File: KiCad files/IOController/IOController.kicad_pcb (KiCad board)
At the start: 2 copper layers, 30 x 74.3 mm, 48 parts, among them IC1 TPS922054DMTR, J1 AVR-ISP-6, J2 XT60 Horizontal Socket, J3 edge connector, Q1 BSS138, SW1 RotaryEncoder_Switch, SW2 TL3342, U1 LP2985-1.8, U3 LP2985-5.0, U4 ATtiny45V-10X

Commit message: updated small changes
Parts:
- added NT1: NetTie, NetTie:NetTie-2_SMD_Pad2.0mm, F.Cu at (37.0, 32.4)
- added R12: 0Ω 0402, Resistor_SMD:R_0402_1005Metric, F.Cu at (20.9, 39.2)
- added R13: 0Ω 0402, Resistor_SMD:R_0402_1005Metric, F.Cu at (21.9, 39.2)
- C14: value 25V 100nF 0402 -> 50V 0.1uF 0805; footprint Capacitor_SMD:C_0402_1005Metric -> Capacitor_SMD:C_0805_2012Metric
- C17: value 16V 2.2uF 0402 -> Csense 50V 2.2uF 0805; footprint Capacitor_SMD:C_0402_1005Metric -> Capacitor_SMD:C_0805_2012Metric
- IC1: value TPS922054DMTR -> TPS923654DMTR
- J1: footprint Connector_PinHeader_1.00mm:PinHeader_2x03_P1.00mm_Vertical -> Connector_PinHeader_2.54mm:PinHeader_2x03_P2.54mm_Vertical
- L1: value VLS6045AF-100M -> SRP1770TA-220M; footprint Inductor_SMD:L_TDK_VLS6045EX_VLS6045AF -> Inductor_SMD:L_Bourns_SRP1770TA_16.9x16.9mm
- R10: value 309K 0402 -> Rovp1 232K 0402
- R11: value 102K 0402 -> Rovp2 10K 0402
- R6: value 52K3 0402 -> Rfset 52K3 0402
- R7: value 61K9 0402 -> Rtemp 61K9 0402
- R8: value 825ohm 0402 -> Rcomp 825ohm 0402
- R9: value 33mΩ 2512 -> Rsense 65mΩ 2512
- SW2: value TL3342 -> B3U; footprint Button_Switch_SMD:SW_SPST_TL3342 -> Button_Switch_SMD:SW_SPST_B3U-1000P-B
- moved C14 22.7 mm to (19.4, 38.5), turned to 90 degrees
- moved C12 22.1 mm to (22.1, 48.6), turned to 180 degrees
- moved R10 21.1 mm to (22.1, 37.8)
- moved C13 20.9 mm to (23.5, 50.0)
- moved R5 20.9 mm to (24.5, 50.0)
- moved R11 20.5 mm to (24.0, 37.8), turned to 180 degrees
- moved IC1 20.3 mm to (23.2, 46.0)
- moved R8 18.3 mm to (23.5, 41.2)
- moved C17 18.3 mm to (17.4, 38.5), turned to 90 degrees
- moved C15 18.0 mm to (24.0, 38.8)
- moved C16 18.0 mm to (24.0, 39.7)
- moved R6 17.5 mm to (24.5, 41.2), turned to 90 degrees
- moved R7 16.5 mm to (25.5, 41.2), turned to 90 degrees
- moved R9 16.1 mm to (19.8, 34.8), turned to 180 degrees
- moved D1 13.7 mm to (17.4, 45.5), turned to 0 degrees
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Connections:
- C14 pad 1: Net-(IC1-CSN) -> Net-(D1-K)
- C14 pad 2: LED_V- -> LED V+
- C17 pad 1: Net-(IC1-CSN) -> Net-(D1-K)
- C17 pad 2: LED_V- -> LED V+
- C18 pad 1: VCC -> LED V+
- C19 pad 1: VCC -> LED V+
- C20 pad 1: VCC -> LED V+
- C21 pad 1: VCC -> LED V+
- C22 pad 1: VCC -> LED V+
- C23 pad 1: VCC -> LED V+
- D1 pad 3: VCC -> Net-(D1-K)
- IC1 pad 12: LED_V- -> Net-(IC1-CSP)
- J1 pad 3: ROT_A -> SW1
- J3 pad 1: VCC -> LED V+
- L1 pad 1: Net-(IC1-SW) -> VCC
- L1 pad 2: Net-(IC1-CSN) -> Net-(IC1-SW)
- R10 pad 2: LED_V- -> LED V+
- R9 pad 1: Net-(IC1-CSN) -> Net-(D1-K)
- R9 pad 2: LED_V- -> LED V+
- U4 pad 3: SW1 -> ROT_A
- U4 pad 7: ROT_A -> SW1
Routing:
- net LED V+: track 0.00 -> 41.0 mm, vias 0 -> 2
- net Net-(D1-K): track 0.00 -> 23.9 mm, vias 0 -> 3
- net Net-(IC1-CSN): track 27.4 -> 5.20 mm
- net SW1: track 20.0 -> 38.3 mm, vias 2 -> 4
- net ROT_SW1: track 29.4 -> 46.3 mm
- net +1V8: track 36.8 -> 53.6 mm
- net VCC: track 101.9 -> 85.8 mm, vias 341 -> 0
- net Net-(IC1-FSET): track 18.3 -> 2.85 mm
- net GND: track 9.53 -> 22.3 mm, vias 205 -> 22
- net Net-(IC1-TEMP): track 15.8 -> 2.98 mm
- net LED_V-: track 34.3 -> 23.7 mm
- net Net-(IC1-COMP): track 12.4 -> 2.98 mm
- net Net-(IC1-SW): track 14.9 -> 23.2 mm, vias 0 -> 2
- net Net-(J1-~{RST}): track 3.56 -> 11.1 mm, vias 0 -> 2
- net Net-(C15-Pad1): track 8.88 -> 1.94 mm
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- removed copper zone on F.Cu, net LED_V-
- removed copper zone on B.Cu, net VCC
- removed copper zone on F.Cu, net VCC

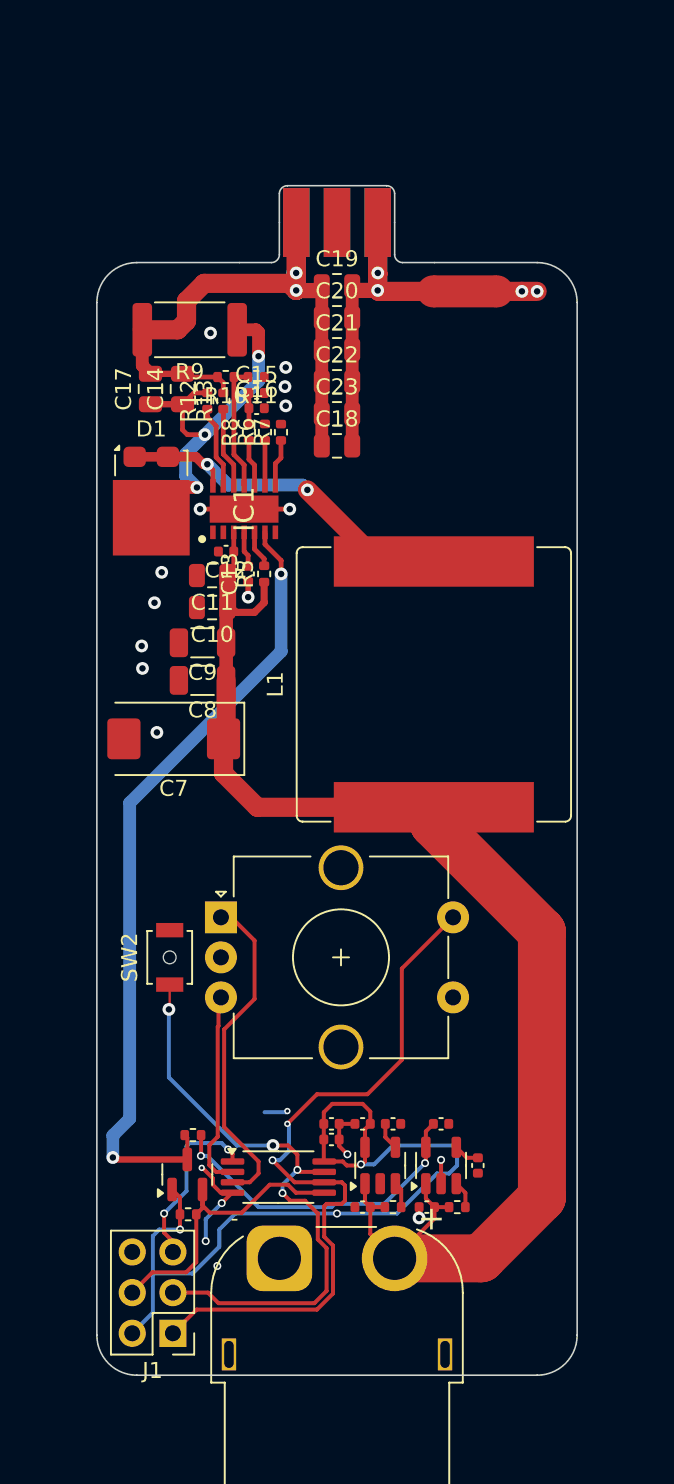
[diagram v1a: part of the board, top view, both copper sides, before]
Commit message: re-organised some files, started work on implementing 100W and 240W EPR versions of the charge board
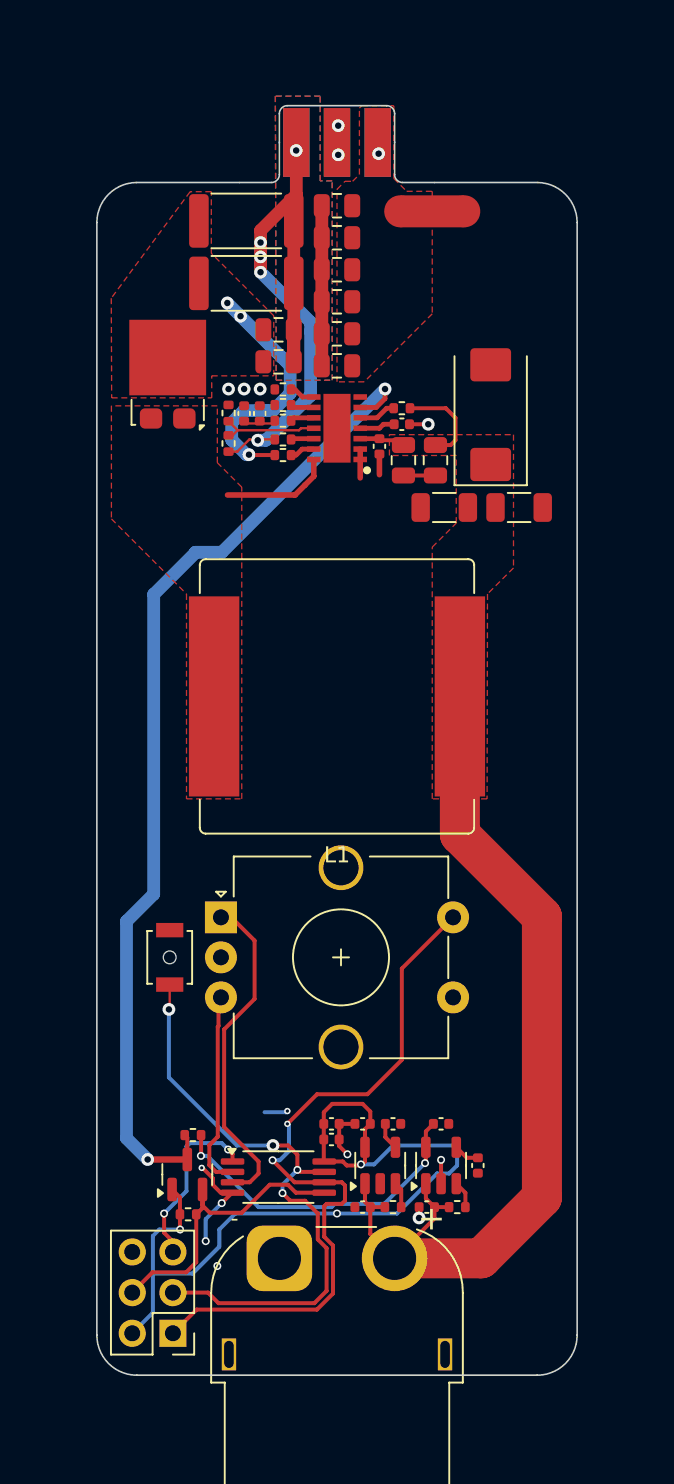
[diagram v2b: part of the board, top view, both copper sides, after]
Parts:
- added R14: 2512 120mR, Resistor_SMD:R_2512_6332Metric, F.Cu at (23.3, 31.9)
- C17: value Csense 50V 2.2uF 0805 -> Csense 50V 30uF 0805
- R10: value Rovp1 232K 0402 -> Rovp1 200K 0402
- R6: value Rfset 52K3 0402 -> Rfset 160K 0402
- R7: value Rtemp 61K9 0402 -> Rtemp 57K6 0402
- R9: value Rsense 65mΩ 2512 -> 2512 120mR
- moved C7 28.3 mm to (38.6, 40.1), turned to 90 degrees
- moved C9 21.5 mm to (40.4, 45.9), turned to 0 degrees
- moved C8 18.6 mm to (35.7, 45.9)
- moved C10 16.7 mm to (35.1, 43.0), turned to -90 degrees
- moved C11 14.0 mm to (33.1, 43.0), turned to -90 degrees
- moved R5 13.5 mm to (33.0, 39.7), turned to 180 degrees
- moved C13 13.4 mm to (33.0, 40.7), turned to 180 degrees
- moved C12 11.6 mm to (31.6, 42.1), turned to -90 degrees
- moved C17 8.81 mm to (25.4, 34.8), turned to 0 degrees
- moved D1 7.99 mm to (18.4, 37.6), turned to 180 degrees
- moved IC1 7.69 mm to (29.0, 41.0), turned to 180 degrees
- moved R9 7.67 mm to (23.3, 28.0), turned to 0 degrees
- moved C14 6.24 mm to (25.4, 36.8), turned to 0 degrees
- moved L1 6.10 mm to (29.0, 57.7), turned to 180 degrees
- moved R12 5.81 mm to (25.6, 42.6), turned to 180 degrees
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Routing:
- net LED_V-: track 23.7 -> 0.00 mm, vias 2 -> 1
- net VCC: track 85.8 -> 66.1 mm
- net Net-(IC1-SW): track 23.2 -> 6.92 mm, vias 2 -> 0
- net LED_PWM_5V: track 50.1 -> 62.8 mm
- net Net-(D1-K): track 23.9 -> 15.8 mm
- net LED V+: track 41.0 -> 48.8 mm, vias 2 -> 5
- net Net-(IC1-CSN): track 5.20 -> 1.57 mm
- net Net-(IC1-CSP): track 5.06 -> 1.44 mm
- net GND: track 22.3 -> 19.5 mm, vias 22 -> 12
- net Net-(IC1-UVP): track 7.95 -> 6.31 mm
- net Net-(IC1-COMP): track 2.98 -> 1.49 mm
- net Net-(IC1-TEMP): track 2.98 -> 1.61 mm
- net Net-(IC1-FSET): track 2.85 -> 1.48 mm
- net unconnected-(J3-Pin_2-Pad2): vias 0 -> 2
- added copper zone on B.Cu, net LED V+
- added copper zone on F.Cu, net LED V+
- added copper zone on F.Cu, net LED_V-
- added copper zone on F.Cu, net Net-(D1-K)
- added copper zone on F.Cu, net Net-(IC1-SW)
- added copper zone on F.Cu, net VCC
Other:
- board size 30 x 74.3 mm -> 30 x 79.3 mm

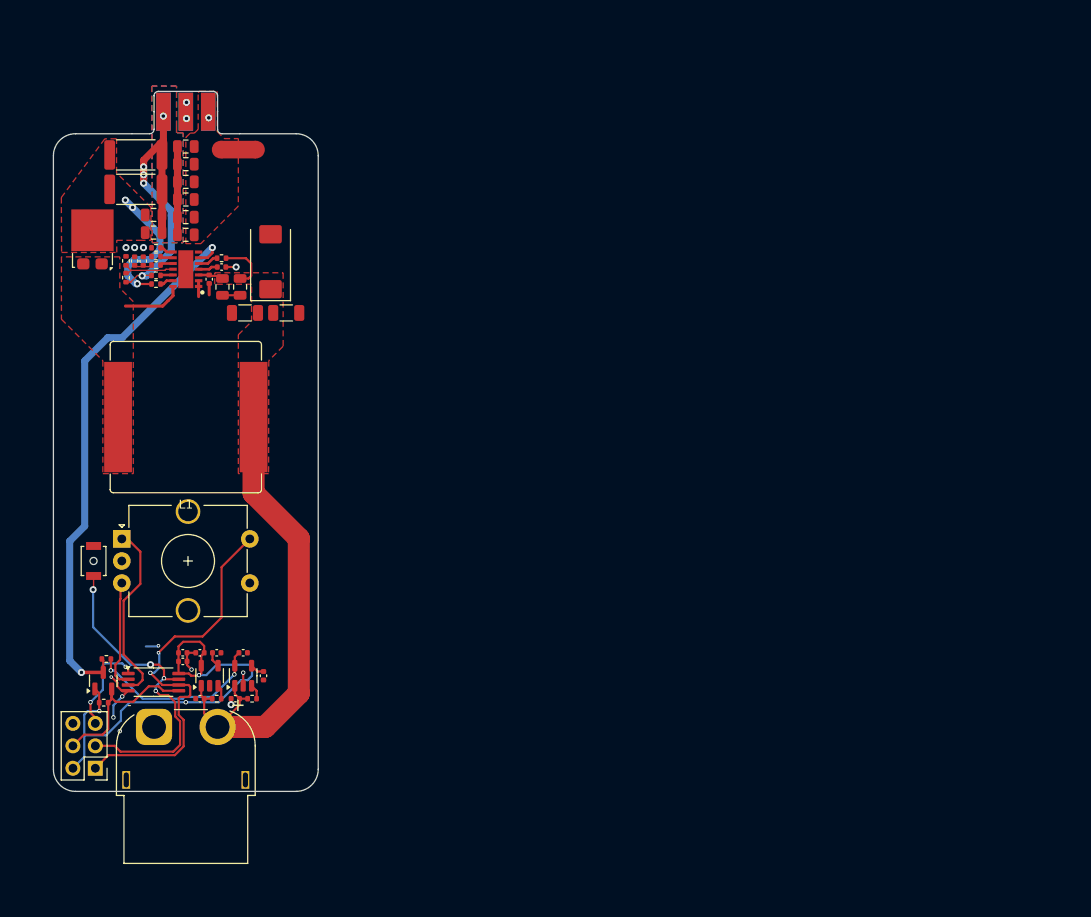
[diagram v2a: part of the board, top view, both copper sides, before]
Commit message: swapped RP2040 for attiny1634, still requires more work.
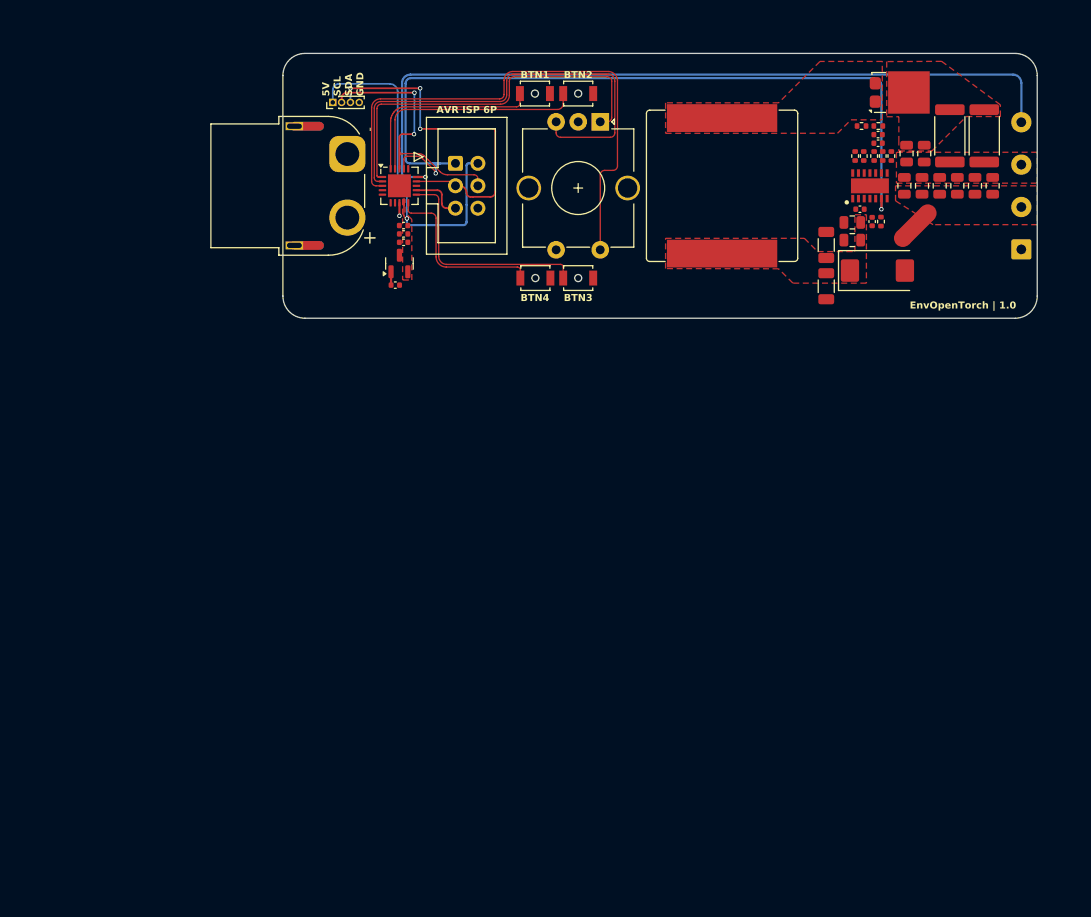
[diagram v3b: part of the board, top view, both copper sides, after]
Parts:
- removed C24: 0.1uF 0402, Capacitor_SMD:C_0402_1005Metric
- removed C25: 1uF 0402, Capacitor_SMD:C_0402_1005Metric
- removed C5: 10nF 0402, Capacitor_SMD:C_0402_1005Metric
- removed C6: 2.2uF 0402, Capacitor_SMD:C_0402_1005Metric
- removed Q1: BSS138, Package_TO_SOT_SMD:SOT-23
- removed R1, R2, R3, R4: 10K 0402, Resistor_SMD:R_0402_1005Metric
- removed SW2: B3U, Button_Switch_SMD:SW_SPST_B3U-1000P-B
- removed U3: LP2985-5.0, Package_TO_SOT_SMD:SOT-23-5
- removed U4: ATtiny45V-10X, Package_SO:TSSOP-8_4.4x3mm_P0.65mm
- added J101: Conn_01x04, Connector_Wire:SolderWire-0.5sqmm_1x04_P4.8mm_D0.9mm_OD2.3mm, F.Cu at (123.7, 38.7)
- added SW101: B3U, Button_Switch_SMD:SW_SPST_B3U-1000P-B, F.Cu at (68.5, 21.1)
- added SW102: B3U, Button_Switch_SMD:SW_SPST_B3U-1000P-B, F.Cu at (73.5, 21.1)
- added SW103: B3U, Button_Switch_SMD:SW_SPST_B3U-1000P-B, F.Cu at (73.5, 42.0)
- added SW104: B3U, Button_Switch_SMD:SW_SPST_B3U-1000P-B, F.Cu at (68.6, 42.0)
- added U2: ATtiny1634-M, Package_DFN_QFN:QFN-20-1EP_4x4mm_P0.5mm_EP2.6x2.6mm, F.Cu at (53.2, 31.5)
- C1: value 1uF 0402 -> 0401 1uF 35V
- C2: value 10nF 0402 -> 0401 2.2uF 6.3V
- C3: value 2.2uF 0402 -> 0401 1uF 6.3V
- C4: value 1uF 0402 -> 0401 10uF 6.3V
- J1: footprint Connector_PinHeader_2.54mm:PinHeader_2x03_P2.54mm_Vertical -> Connector_IDC:IDC-Header_2x03_P2.54mm_Vertical
- J3: value edge connector -> Conn_01x04; footprint EnvExtras:CardEdge1x03 -> Connector_PinHeader_1.00mm:PinHeader_1x04_P1.00mm_Vertical
- L1: value SRP1770TA-220M -> SRP1770TA-100M
- SW1: value RotaryEncoder_Switch -> EC12
- U1: value LP2985-1.8 -> AP7384-50SA; footprint Package_TO_SOT_SMD:SOT-23-5 -> Package_TO_SOT_SMD:SOT-23
- moved R9 96.1 mm to (119.5, 25.8), turned to -90 degrees
- moved D1 93.0 mm to (109.9, 20.9), turned to 90 degrees
- moved R14 92.4 mm to (115.5, 25.8), turned to -90 degrees
- moved C19 91.5 mm to (120.4, 31.5), turned to -90 degrees
- moved C20 89.4 mm to (118.4, 31.5), turned to -90 degrees
- moved C17 87.6 mm to (112.7, 27.9), turned to -90 degrees
- moved C21 87.4 mm to (116.4, 31.5), turned to -90 degrees
- moved R11 86.6 mm to (107.5, 24.7), turned to 180 degrees
- moved C14 85.8 mm to (110.7, 27.9), turned to -90 degrees
- moved C15 85.4 mm to (107.4, 25.7), turned to 0 degrees
- moved C22 85.4 mm to (114.4, 31.5), turned to -90 degrees
- moved R10 85.1 mm to (105.5, 24.7), turned to 180 degrees
- moved C16 84.3 mm to (107.4, 26.7), turned to 0 degrees
- moved R7 83.9 mm to (108.9, 28.1), turned to 90 degrees
- moved C23 83.5 mm to (112.4, 31.5), turned to -90 degrees
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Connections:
- C2 pad 1: Net-(U1-BP) -> +5V
- C3 pad 1: +1V8 -> +5V
- C4 pad 1: VCC -> +5V
- IC1 pad 7: unconnected-(IC1-FAULT-Pad7) -> GND
- J1 pad 1: ROT_SW1 -> LED_PWM_5V
- J1 pad 2: +1V8 -> +5V
- J1 pad 3: SW1 -> SCL
- J1 pad 4: LED_PWM_1V8 -> SDA
- J1 pad 5: Net-(J1-~{RST}) -> /MCU/PC3
- J3 pad 1: LED V+ -> +5V
- J3 pad 2: unconnected-(J3-Pin_2-Pad2) -> SDA
- J3 pad 3: LED_V- -> SCL
- SW1 pad S1: ROT_SW1 -> BTN5
- U1 pad 2: GND -> +5V
- U1 pad 3: Net-(U1-ON/~{OFF}) -> GND
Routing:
- net therm1_adc: track 0.00 -> 89.7 mm, vias 0 -> 1
- net VCC: track 66.1 -> 1.51 mm
- net BTN5: track 0.00 -> 61.8 mm
- net +1V8: track 53.6 -> 0.00 mm, vias 3 -> 0
- net LED V+: track 48.8 -> 0.00 mm, vias 5 -> 0
- net ROT_SW1: track 46.3 -> 0.00 mm, vias 2 -> 0
- net ROT_B: track 12.4 -> 53.8 mm
- net SCL: track 0.00 -> 39.8 mm, vias 0 -> 3
- net SW1: track 38.3 -> 0.00 mm, vias 4 -> 0
- net SDA: track 0.00 -> 32.4 mm, vias 0 -> 2
- net LED_PWM_5V: track 62.8 -> 92.0 mm
- net BTN2: track 0.00 -> 26.8 mm
- net BTN3: track 0.00 -> 25.3 mm
- net ROT_A: track 20.8 -> 43.5 mm
- net BTN1: track 0.00 -> 22.3 mm
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- added copper zone on F.Cu, net +5V
- removed copper zone on B.Cu, net LED V+
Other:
- board size 30 x 79.3 mm -> 85.5 x 30 mm
- board text added: "5V SCL SDA GND"
- board text added: "AVR ISP 6P"
- board text added: "BTN1"
- board text added: "BTN2"
- board text added: "BTN3"
- board text added: "BTN4"
- board text added: "EnvOpenTorch | 1.0"
